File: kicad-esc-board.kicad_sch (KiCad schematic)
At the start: 9 parts, among them J1 PhoenixContact_01x03_WireToBo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, J2 PhoenixContact_01x02_WireToBo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, J3 Conn_01x01, J4 JST_01x02_TH_Vertical, J5 JST_01x02_TH_Vertical, M1 Blue Robotics Basic ESC

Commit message: Added the double pin header for logic analyzer testing and doubled up on power traces.
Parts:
- removed J3: Conn_01x01, Connector_PinHeader_2.54mm:PinHeader_1x01_P2.54mm_Vertical, symbol Connector_Generic:Conn_01x01
- added J6: JST_01x02_TH_Vertical, Connector_PinHeader_2.00mm:PinHeader_1x02_P2.00mm_Vertical, symbol esc_board_custom_symbols:JST_01x02_TH_Vertical
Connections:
- net PWM-Ctrl: now also J6.2 (Pin_2)
- net PWM-GND: now also J6.1 (Pin_1)
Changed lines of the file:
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@@
+	)
+	(junction
+		(at 59.69 66.04)
+		(diameter 0)
+		(color 0 0 0 0)
 	)
 	(junction
@@
 	(wire
 		(pts
+			(xy 59.69 66.04) (xy 73.66 66.04)
+		)
+		(stroke
+			(width 0)
+			(type default)
+		)
+	)
+	(wire
+		(pts
 			(xy 44.45 69.85) (xy 44.45 66.04)
 		)
@@
 	(wire
 		(pts
+			(xy 59.69 62.23) (xy 59.69 66.04)
+		)
+		(stroke
+			(width 0)
+			(type default)
+		)
+	)
+	(wire
+		(pts
 			(xy 134.62 52.07) (xy 140.97 52.07)
 		)
@@
 	(wire
 		(pts
-			(xy 44.45 66.04) (xy 73.66 66.04)
+			(xy 44.45 66.04) (xy 59.69 66.04)
 		)
 		(stroke
@@
 	)
 	(symbol
-		(lib_id "Connector_Generic:Conn_01x01")
-		(at 57.15 57.15 90)
-		(unit 1)
-		(body_style 1)
-		(exclude_from_sim no)
-		(in_bom yes)
-		(on_board yes)
-		(in_pos_files yes)
-		(dnp no)
-		(fields_autoplaced yes)
-		(property "Reference" "J3"
-			(at 59.69 55.8799 90)
-			(show_name no)
-			(do_not_autoplace no)
-			(effects
-				(font
-					(size 1.27 1.27)
-				)
-				(justify right)
-			)
-		)
-		(property "Value" "Conn_01x01"
-			(at 59.69 58.4199 90)
-			(show_name no)
-			(do_not_autoplace no)
-			(effects
-				(font
-					(size 1.27 1.27)
-				)
-				(justify right)
-			)
-		)
-		(property "Footprint" "Connector_PinHeader_2.54mm:PinHeader_1x01_P2.54mm_Vertical"
-			(at 57.15 57.15 0)
-			(hide yes)
-			(show_name no)
-			(do_not_autoplace no)
-			(effects
-				(font
-					(size 1.27 1.27)
-				)
-			)
-		)
-		(property "Datasheet" ""
-			(at 57.15 57.15 0)
-			(hide yes)
-			(show_name no)
-			(do_not_autoplace no)
-			(effects
-				(font
-					(size 1.27 1.27)
-				)
-			)
-		)
-		(property "Description" "Generic connector, single row, 01x01, script generated (kicad-library-utils/schlib/autogen/connector/)"
-			(at 57.15 57.15 0)
-			(hide yes)
-			(show_name no)
-			(do_not_autoplace no)
-			(effects
-				(font
-					(size 1.27 1.27)
-				)
-			)
-		)
-		(pin "1"
-		)
-		(instances
-			(project "kicad-esc-board"
-				(path "/4e280a3c-f245-4f61-bab7-25e6d294ade1"
-					(reference "J3")
-					(unit 1)
-				)
-			)
-		)
-	)
-	(symbol
 		(lib_id "power:GND")
 		(at 88.9 50.8 0)
@@
 					(unit 1)
 				)
+			)
+		)
+	)
+	(symbol
+		(lib_id "esc_board_custom_symbols:JST_01x02_TH_Vertical")
+		(at 59.69 57.15 270)
+		(mirror x)
+		(unit 1)
+		(body_style 1)
+		(exclude_from_sim no)
+		(in_bom yes)
+		(on_board yes)
+		(in_pos_files yes)
+		(dnp no)
+		(property "Reference" "J6"
+			(at 62.738 57.912 90)
+			(show_name no)
+			(do_not_autoplace no)
+			(effects
+				(font
+					(size 1.27 1.27)
+				)
+				(justify left)
+			)
+		)
+		(property "Value" "JST_01x02_TH_Vertical"
+			(at 62.484 55.88 90)
+			(show_name no)
+			(do_not_autoplace no)
+			(effects
+				(font
+					(size 1.27 1.27)
+				)
+				(justify left)
+			)
+		)
+		(property "Footprint" "Connector_PinHeader_2.00mm:PinHeader_1x02_P2.00mm_Vertical"
+			(at 59.69 57.15 0)
+			(hide yes)
+			(show_name no)
+			(do_not_autoplace no)
+			(effects
+				(font
+					(size 1.27 1.27)
+				)
+			)
+		)
+		(property "Datasheet" "https://www.digikey.com/en/products/detail/jst-sales-america-inc/B2B-PH-K-S/926611"
+			(at 59.69 57.15 0)
+			(hide yes)
+			(show_name no)
+			(do_not_autoplace no)
+			(effects
+				(font
+					(size 1.27 1.27)
+				)
+			)
+		)
+		(property "Description" "https://www.digikey.com/en/products/detail/jst-sales-america-inc/B2B-PH-K-S/926611"
+			(at 55.118 9.906 0)
+			(hide yes)
+			(show_name no)
+			(do_not_autoplace no)
+			(effects
+				(font
+					(size 1.27 1.27)
+				)
+			)
+		)
+		(pin "1"
+		)
+		(pin "2"
+		)
+		(instances
+			(project "kicad-esc-board"
+				(path "/4e280a3c-f245-4f61-bab7-25e6d294ade1"
+					(reference "J6")
+					(unit 1)
+				)

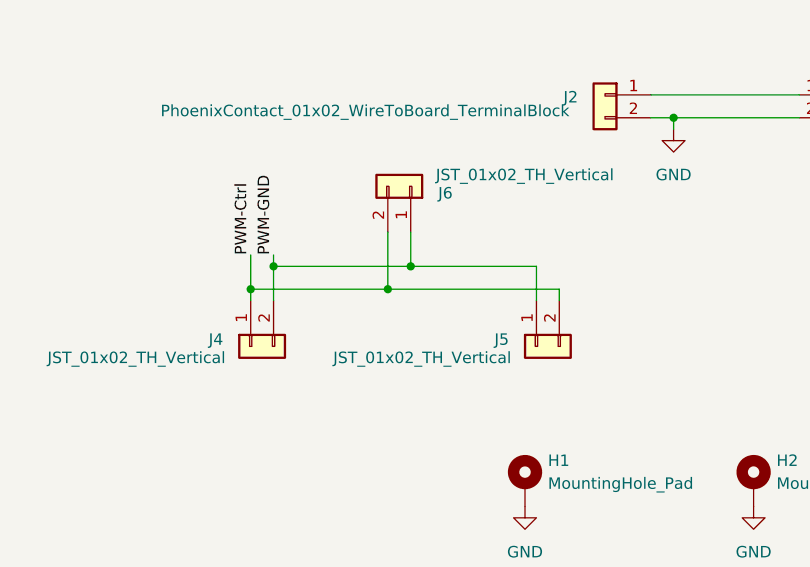
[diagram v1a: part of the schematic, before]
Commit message: made some final tweaks with net labels.
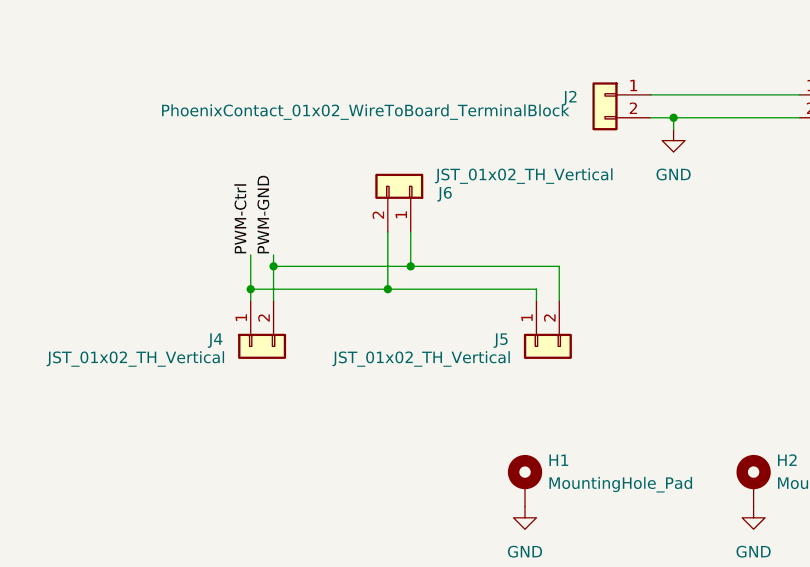
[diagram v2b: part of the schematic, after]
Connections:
- net PWM-Ctrl: now also J5.1 (Pin_1); no longer J5.2 (Pin_2)
- net PWM-GND: now also J5.2 (Pin_2); no longer J5.1 (Pin_1)
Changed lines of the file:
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@@
 	(wire
 		(pts
-			(xy 59.69 66.04) (xy 73.66 66.04)
+			(xy 59.69 66.04) (xy 76.2 66.04)
 		)
 		(stroke
@@
 	(wire
 		(pts
-			(xy 57.15 68.58) (xy 41.91 68.58)
+			(xy 41.91 68.58) (xy 73.66 68.58)
 		)
 		(stroke
@@
 		(pts
 			(xy 86.36 46.99) (xy 102.87 46.99)
-		)
-		(stroke
-			(width 0)
-			(type default)
-		)
-	)
-	(wire
-		(pts
-			(xy 76.2 68.58) (xy 57.15 68.58)
 		)
 		(stroke
@@
 		(pts
 			(xy 88.9 49.53) (xy 102.87 49.53)
+		)
+		(stroke
+			(width 0)
+			(type default)
+		)
+	)
+	(wire
+		(pts
+			(xy 76.2 66.04) (xy 76.2 69.85)
+		)
+		(stroke
+			(width 0)
+			(type default)
+		)
+	)
+	(wire
+		(pts
+			(xy 73.66 68.58) (xy 73.66 69.85)
 		)
 		(stroke
@@
 	(wire
 		(pts
-			(xy 73.66 66.04) (xy 73.66 69.85)
-		)
-		(stroke
-			(width 0)
-			(type default)
-		)
-	)
-	(wire
-		(pts
 			(xy 44.45 66.04) (xy 59.69 66.04)
 		)
@@
 		)
 		(stroke
-			(width 0)
-			(type default)
-		)
-	)
-	(wire
-		(pts
-			(xy 76.2 69.85) (xy 76.2 68.58)
-		)
-		(stroke

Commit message: made common grounds between PWM connections and board.
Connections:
- net PWM-GND is gone; now on net GND: J4.2 (Pin_2), J5.2 (Pin_2), J6.1 (Pin_1)
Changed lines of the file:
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@@
+	(wire
+		(pts
+			(xy 33.02 95.25) (xy 48.26 95.25)
+		)
+		(stroke
+			(width 0)
+			(type default)
+		)
+	)
 	(wire
 		(pts
@@
 	(wire
 		(pts
+			(xy 48.26 95.25) (xy 48.26 99.06)
+		)
+		(stroke
+			(width 0)
+			(type default)
+		)
+	)
+	(wire
+		(pts
 			(xy 76.2 66.04) (xy 76.2 69.85)
 		)
@@
 		(pts
 			(xy 86.36 49.53) (xy 88.9 49.53)
+		)
+		(stroke
+			(width 0)
+			(type default)
+		)
+	)
+	(wire
+		(pts
+			(xy 33.02 99.06) (xy 33.02 95.25)
 		)
 		(stroke
@@
 	(symbol
 		(lib_id "power:GND")
+		(at 33.02 99.06 0)
+		(unit 1)
+		(body_style 1)
+		(exclude_from_sim no)
+		(in_bom yes)
+		(on_board yes)
+		(in_pos_files yes)
+		(dnp no)
+		(fields_autoplaced yes)
+		(property "Reference" "#PWR06"
+			(at 33.02 105.41 0)
+			(hide yes)
+			(show_name no)
+			(do_not_autoplace no)
+			(effects
+				(font
+					(size 1.27 1.27)
+				)
+			)
+		)
+		(property "Value" "GND"
+			(at 33.02 104.14 0)
+			(show_name no)
+			(do_not_autoplace no)
+			(effects
+				(font
+					(size 1.27 1.27)
+				)
+			)
+		)
+		(property "Footprint" ""
+			(at 33.02 99.06 0)
+			(hide yes)
+			(show_name no)
+			(do_not_autoplace no)
+			(effects
+				(font
+					(size 1.27 1.27)
+				)
+			)
+		)
+		(property "Datasheet" ""
+			(at 33.02 99.06 0)
+			(hide yes)
+			(show_name no)
+			(do_not_autoplace no)
+			(effects
+				(font
+					(size 1.27 1.27)
+				)
+			)
+		)
+		(property "Description" "Power symbol creates a global label with name \"GND\" , ground"
+			(at 33.02 99.06 0)
+			(hide yes)
+			(show_name no)
+			(do_not_autoplace no)
+			(effects
+				(font
+					(size 1.27 1.27)
+				)
+			)
+		)
+		(pin "1"
+		)
+		(instances
+			(project "kicad-esc-board"
+				(path "/4e280a3c-f245-4f61-bab7-25e6d294ade1"
+					(reference "#PWR06")
+					(unit 1)
+				)
+			)
+		)
+	)
+	(symbol
+		(lib_id "power:GND")
 		(at 119.38 64.77 0)
 		(unit 1)
@@
 					(unit 1)
 				)
+			)
+		)
+	)
+	(symbol
+		(lib_id "power:GND")
+		(at 48.26 99.06 0)
+		(unit 1)
+		(body_style 1)
+		(exclude_from_sim no)
+		(in_bom yes)
+		(on_board yes)
+		(in_pos_files yes)
+		(dnp no)
+		(fields_autoplaced yes)
+		(property "Reference" "#PWR07"
+			(at 48.26 105.41 0)
+			(hide yes)
+			(show_name no)
+			(do_not_autoplace no)
+			(effects
+				(font
+					(size 1.27 1.27)
+				)
+			)
+		)
+		(property "Value" "PWM-GND"
+			(at 48.26 104.14 0)
+			(show_name no)
+			(do_not_autoplace no)
+			(effects
+				(font
+					(size 1.27 1.27)
+				)
+			)
+		)
+		(property "Footprint" ""
+			(at 48.26 99.06 0)
+			(hide yes)
+			(show_name no)
+			(do_not_autoplace no)
+			(effects
+				(font
+					(size 1.27 1.27)
+				)
+			)
+		)
+		(property "Datasheet" ""
+			(at 48.26 99.06 0)
+			(hide yes)
+			(show_name no)
+			(do_not_autoplace no)
+			(effects
+				(font
+					(size 1.27 1.27)
+				)
+			)
+		)
+		(property "Description" "Power symbol creates a global label with name \"GND\" , ground"
+			(at 48.26 99.06 0)
+			(hide yes)
+			(show_name no)
+			(do_not_autoplace no)
+			(effects
+				(font
+					(size 1.27 1.27)
+				)
+			)
+		)
+		(pin "1"
+		)
+		(instances
+			(project "kicad-esc-board"
+				(path "/4e280a3c-f245-4f61-bab7-25e6d294ade1"
+					(reference "#PWR07")
+					(unit 1)
+				)
